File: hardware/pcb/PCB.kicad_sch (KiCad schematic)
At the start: 47 parts, among them J1 USB_A, J2 AudioJack3, J3 USB_B_Micro, Q1 BSS138, Q2 MMBT3904, Q3 MMBT3904, SW1 RESET, SW2 S4, SW3 BOOT, SW4 RESET, U1 ESP32-S3-WROOM-1, U2 LM3525M-H, U3 D52Q, U4 CP2102N-Axx-xQFN24, U5 AP7361C-33E, U6 SP0506BAATG

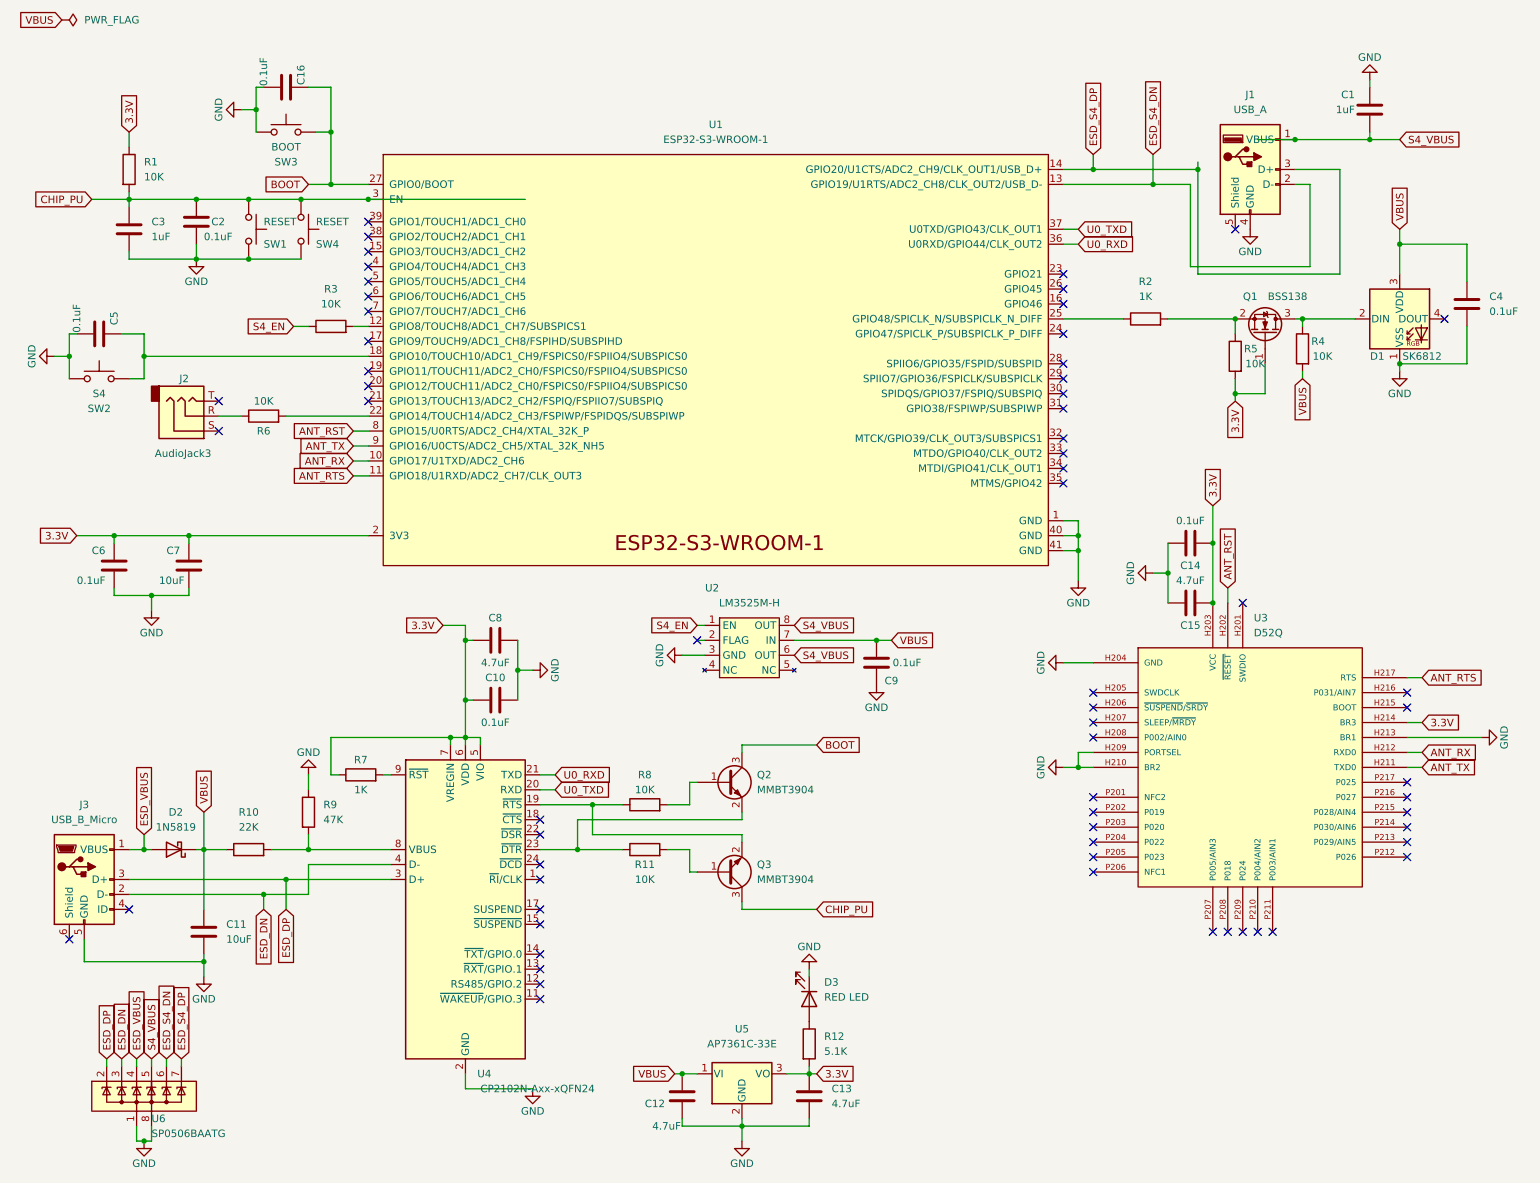
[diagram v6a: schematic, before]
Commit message: update idf sdk compatibility
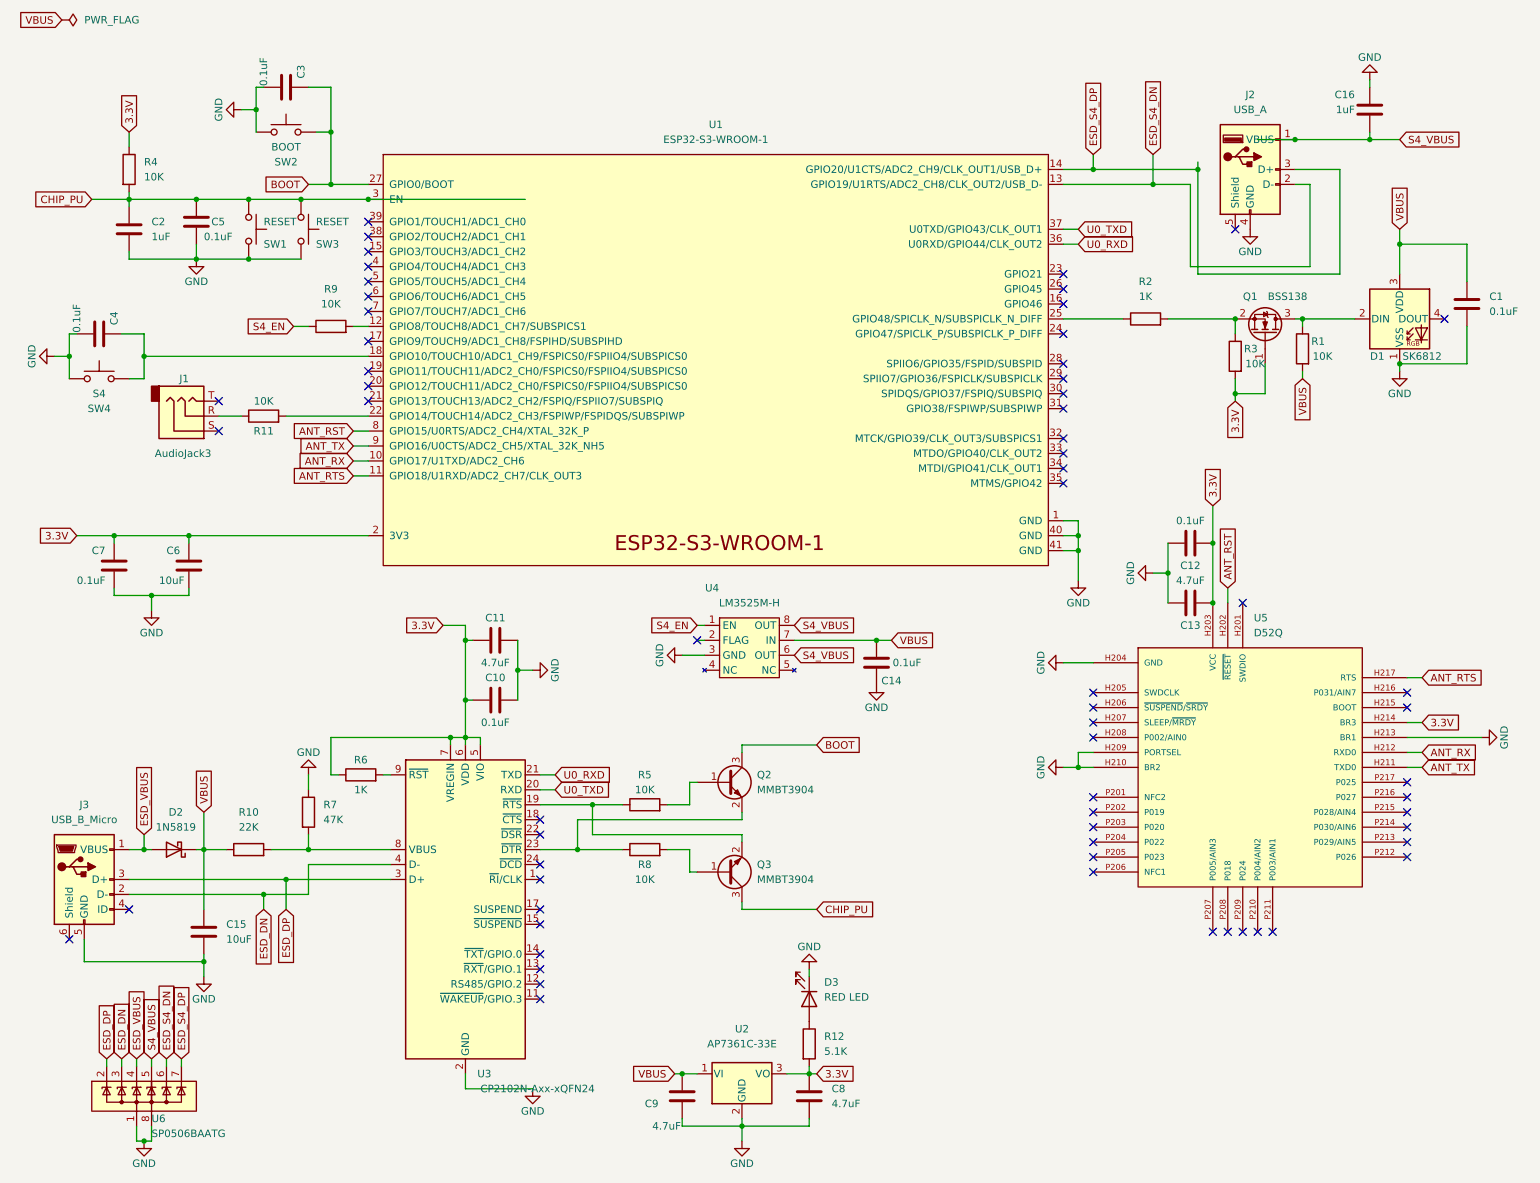
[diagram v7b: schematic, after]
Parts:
- D3: footprint Capacitor_SMD:C_0603_1608Metric_Pad1.08x0.95mm_HandSolder -> LED_SMD:LED_0603_1608Metric_Pad1.05x0.95mm_HandSolder
- renumbered C4 to C1, C8 to C11, C14 to C12, C15 to C13, C9 to C14, C11 to C15, C1 to C16, C3 to C2, C16 to C3, C5 to C4, C2 to C5, C7 to C6, C6 to C7, C13 to C8, C12 to C9, J2 to J1, J1 to J2, R4 to R1, R6 to R11, R5 to R3, R1 to R4, R8 to R5, R7 to R6, R9 to R7, R11 to R8, R3 to R9, SW3 to SW2, SW4 to SW3, SW2 to SW4, U5 to U2, U4 to U3, U2 to U4, U3 to U5
